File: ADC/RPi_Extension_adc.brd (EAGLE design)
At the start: 63 x 50 mm, 39 parts, among them U1 74AHC1G04GW/T1, U2 ADR423ARZ, U3 AD7616BSTZ

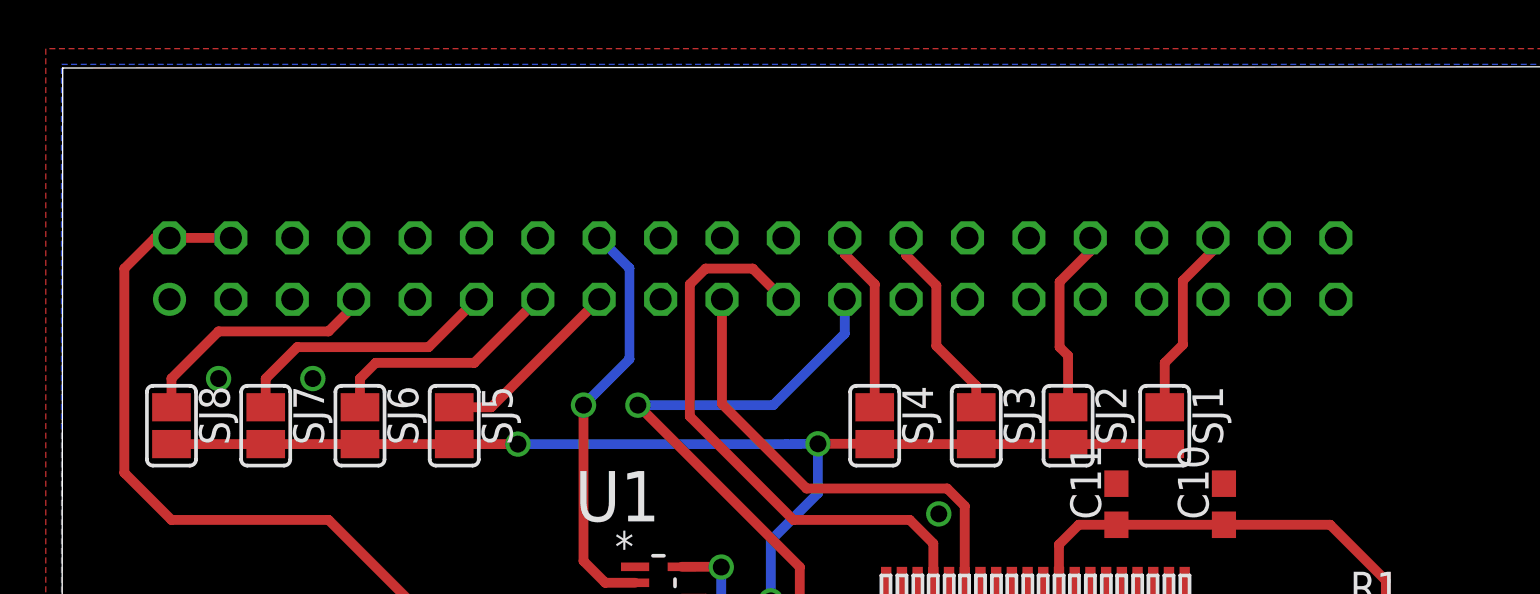
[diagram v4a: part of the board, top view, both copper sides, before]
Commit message: added additional id jumpers to adc and dac board
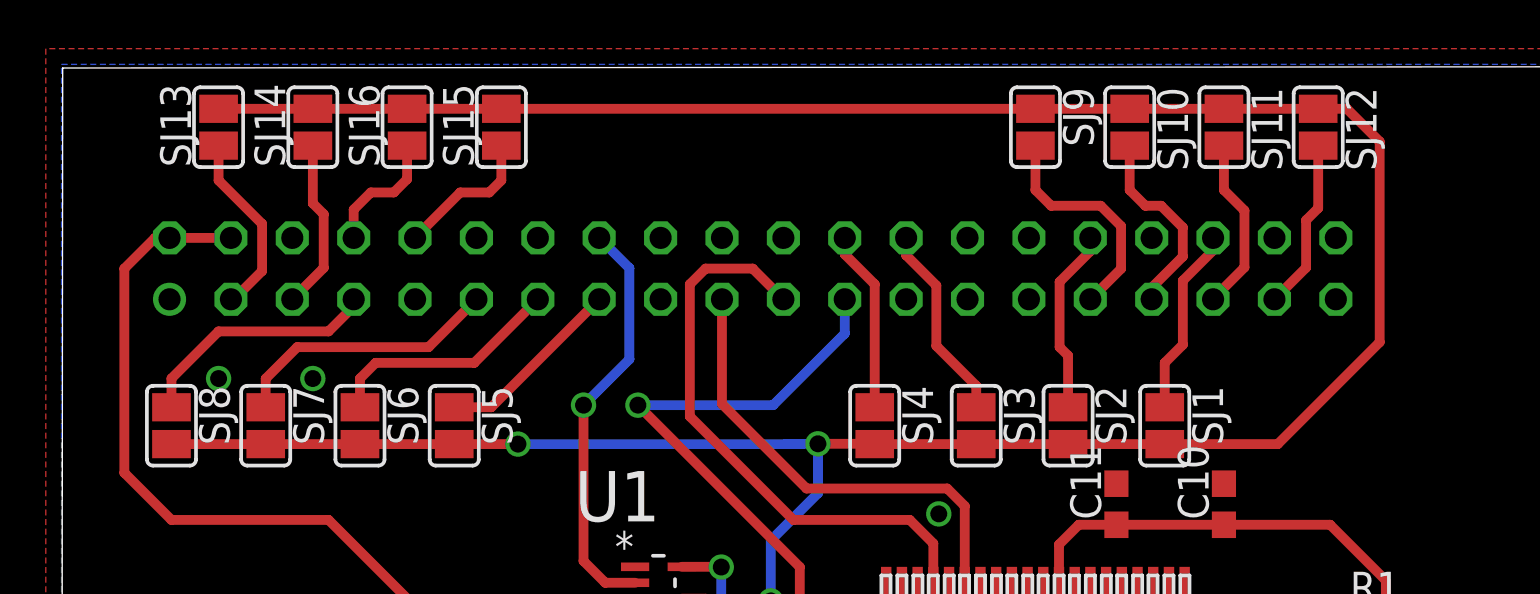
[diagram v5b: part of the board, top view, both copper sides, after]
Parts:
- added SJ10, SJ11, SJ12, SJ13, SJ14, SJ15, SJ16, SJ9: (no value), jumper:SJ
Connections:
- new net N$11: SJ15.1, SV5.10
- new net N$12: SJ9.2, SV5.31
- new net N$13: SJ10.2, SV5.33
- new net N$14: SJ11.2, SV5.35
- new net N$15: SJ12.2, SV5.37
- new net N$5: SJ13.1, SV5.3
- new net N$8: SJ14.1, SV5.5
- new net N$9: SJ16.1, SV5.8
- net SYNC: now also SJ10.1, SJ11.1, SJ12.1, SJ13.2, SJ14.2, SJ15.2, SJ16.2, SJ9.1
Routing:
- net SYNC: track 53.2 -> 120.7 mm
- net N$12: track 0.00 -> 9.56 mm
- net N$13: track 0.00 -> 8.18 mm
- net N$5: track 0.00 -> 7.71 mm
- net N$14: track 0.00 -> 7.25 mm
- net N$15: track 0.00 -> 7.11 mm
- net N$8: track 0.00 -> 7.08 mm
- net N$11: track 0.00 -> 6.00 mm
- net N$9: track 0.00 -> 5.29 mm
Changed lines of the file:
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@@
 <attribute name="OC_NEWARK" value="99K0513" x="24.7" y="28.6" size="1.778" layer="27" display="off"/>
 </element>
+<element name="SJ9" library="jumper" package="SJ" value="" x="40.3" y="47.45" rot="R270"/>
+<element name="SJ10" library="jumper" package="SJ" value="" x="44.2" y="47.45" rot="R270"/>
+<element name="SJ11" library="jumper" package="SJ" value="" x="48.1" y="47.45" rot="R270"/>
+<element name="SJ12" library="jumper" package="SJ" value="" x="52" y="47.45" rot="R270"/>
+<element name="SJ13" library="jumper" package="SJ" value="" x="6.5" y="47.45" rot="R90"/>
+<element name="SJ14" library="jumper" package="SJ" value="" x="10.4" y="47.45" rot="R90"/>
+<element name="SJ15" library="jumper" package="SJ" value="" x="18.2" y="47.45" rot="R90"/>
+<element name="SJ16" library="jumper" package="SJ" value="" x="14.3" y="47.45" rot="R90"/>
 </elements>
 <signals>
@@
 <wire x1="31.3" y1="32.3" x2="29.35" y2="30.35" width="0.4064" layer="16"/>
 <wire x1="29.35" y1="30.35" x2="29.35" y2="27.85" width="0.4064" layer="16"/>
+<contactref element="SJ14" pad="2"/>
+<contactref element="SJ15" pad="2"/>
+<contactref element="SJ16" pad="2"/>
+<contactref element="SJ13" pad="2"/>
+<contactref element="SJ9" pad="1"/>
+<contactref element="SJ10" pad="1"/>
+<contactref element="SJ11" pad="1"/>
+<contactref element="SJ12" pad="1"/>
+<wire x1="6.5" y1="48.212" x2="10.4" y2="48.212" width="0.4064" layer="1"/>
+<wire x1="10.4" y1="48.212" x2="14.3" y2="48.212" width="0.4064" layer="1"/>
+<wire x1="14.3" y1="48.212" x2="18.2" y2="48.212" width="0.4064" layer="1"/>
+<wire x1="18.2" y1="48.212" x2="40.3" y2="48.212" width="0.4064" layer="1"/>
+<wire x1="40.3" y1="48.212" x2="44.2" y2="48.212" width="0.4064" layer="1"/>
+<wire x1="44.2" y1="48.212" x2="48.1" y2="48.212" width="0.4064" layer="1"/>
+<wire x1="52" y1="48.212" x2="53.188" y2="48.212" width="0.4064" layer="1"/>
+<wire x1="45.65" y1="34.338" x2="50.328315625" y2="34.338" width="0.4064" layer="1"/>
+<wire x1="50.328315625" y1="34.338" x2="54.5448875" y2="38.554571875" width="0.4064" layer="1"/>
+<wire x1="54.5448875" y1="38.554571875" x2="54.5448875" y2="46.8551125" width="0.4064" layer="1"/>
+<wire x1="54.5448875" y1="46.8551125" x2="53.188" y2="48.212" width="0.4064" layer="1"/>
+<wire x1="52" y1="48.212" x2="48.1" y2="48.212" width="0.4064" layer="1"/>
 </signal>
 <signal name="N$20">
@@
 <wire x1="30.55" y1="23.05" x2="31.175" y2="22.425" width="0.4064" layer="1"/>
 </signal>
+<signal name="N$5">
+<contactref element="SV5" pad="3"/>
+<contactref element="SJ13" pad="1"/>
+<wire x1="7.01" y1="40.33" x2="7.13" y2="40.33" width="0.4064" layer="1"/>
+<wire x1="7.13" y1="40.33" x2="8.3" y2="41.5" width="0.4064" layer="1"/>
+<wire x1="8.3" y1="41.5" x2="8.3" y2="43.45" width="0.4064" layer="1"/>
+<wire x1="8.3" y1="43.45" x2="6.5" y2="45.25" width="0.4064" layer="1"/>
+<wire x1="6.5" y1="45.25" x2="6.5" y2="46.688" width="0.4064" layer="1"/>
+</signal>
+<signal name="N$8">
+<contactref element="SV5" pad="5"/>
+<contactref element="SJ14" pad="1"/>
+<wire x1="10.4" y1="46.688" x2="10.4" y2="44.3" width="0.4064" layer="1"/>
+<wire x1="10.4" y1="44.3" x2="10.85" y2="43.85" width="0.4064" layer="1"/>
+<wire x1="10.85" y1="43.85" x2="10.85" y2="41.63" width="0.4064" layer="1"/>
+<wire x1="10.85" y1="41.63" x2="9.55" y2="40.33" width="0.4064" layer="1"/>
+</signal>
+<signal name="N$9">
+<contactref element="SV5" pad="8"/>
+<contactref element="SJ16" pad="1"/>
+<wire x1="12.09" y1="42.87" x2="12.09" y2="44.04" width="0.4064" layer="1"/>
+<wire x1="12.09" y1="44.04" x2="12.8" y2="44.75" width="0.4064" layer="1"/>
+<wire x1="12.8" y1="44.75" x2="13.75" y2="44.75" width="0.4064" layer="1"/>
+<wire x1="13.75" y1="44.75" x2="14.3" y2="45.3" width="0.4064" layer="1"/>
+<wire x1="14.3" y1="45.3" x2="14.3" y2="46.688" width="0.4064" layer="1"/>
+</signal>
+<signal name="N$11">
+<contactref element="SV5" pad="10"/>
+<contactref element="SJ15" pad="1"/>
+<wire x1="14.63" y1="42.87" x2="14.63" y2="42.88" width="0.4064" layer="1"/>
+<wire x1="14.63" y1="42.88" x2="16.5" y2="44.75" width="0.4064" layer="1"/>
+<wire x1="16.5" y1="44.75" x2="17.7" y2="44.75" width="0.4064" layer="1"/>
+<wire x1="17.7" y1="44.75" x2="18.2" y2="45.25" width="0.4064" layer="1"/>
+<wire x1="18.2" y1="45.25" x2="18.2" y2="46.688" width="0.4064" layer="1"/>
+</signal>
+<signal name="N$12">
+<contactref element="SV5" pad="31"/>
+<contactref element="SJ9" pad="2"/>
+<wire x1="42.57" y1="40.33" x2="42.58" y2="40.33" width="0.4064" layer="1"/>
+<wire x1="42.58" y1="40.33" x2="43.842459375" y2="41.592459375" width="0.4064" layer="1"/>
+<wire x1="43.842459375" y1="41.592459375" x2="43.842459375" y2="43.3567875" width="0.4064" layer="1"/>
+<wire x1="43.842459375" y1="43.3567875" x2="42.999246875" y2="44.2" width="0.4064" layer="1"/>
+<wire x1="42.999246875" y1="44.2" x2="40.95" y2="44.2" width="0.4064" layer="1"/>
+<wire x1="40.95" y1="44.2" x2="40.3" y2="44.85" width="0.4064" layer="1"/>
+<wire x1="40.3" y1="44.85" x2="40.3" y2="46.688" width="0.4064" layer="1"/>
+</signal>
+<signal name="N$13">
+<contactref element="SV5" pad="33"/>
+<contactref element="SJ10" pad="2"/>
+<wire x1="45.11" y1="40.33" x2="45.11" y2="40.81" width="0.4064" layer="1"/>
+<wire x1="45.11" y1="40.81" x2="46.397921875" y2="42.097921875" width="0.4064" layer="1"/>
+<wire x1="46.397921875" y1="42.097921875" x2="46.397921875" y2="43.302078125" width="0.4064" layer="1"/>
+<wire x1="46.397921875" y1="43.302078125" x2="45.5" y2="44.2" width="0.4064" layer="1"/>
+<wire x1="45.5" y1="44.2" x2="44.85" y2="44.2" width="0.4064" layer="1"/>
+<wire x1="44.85" y1="44.2" x2="44.2" y2="44.85" width="0.4064" layer="1"/>
+<wire x1="44.2" y1="44.85" x2="44.2" y2="46.688" width="0.4064" layer="1"/>
+</signal>
+<signal name="N$14">
+<contactref element="SV5" pad="35"/>
+<contactref element="SJ11" pad="2"/>
+<wire x1="47.65" y1="40.33" x2="47.65" y2="40.35" width="0.4064" layer="1"/>
+<wire x1="47.65" y1="40.35" x2="48.95" y2="41.65" width="0.4064" layer="1"/>
+<wire x1="48.95" y1="41.65" x2="48.95" y2="44" width="0.4064" layer="1"/>
+<wire x1="48.95" y1="44" x2="48.1" y2="44.85" width="0.4064" layer="1"/>
+<wire x1="48.1" y1="44.85" x2="48.1" y2="46.688" width="0.4064" layer="1"/>
+</signal>
+<signal name="N$15">
+<contactref element="SV5" pad="37"/>
+<contactref element="SJ12" pad="2"/>
+<wire x1="52" y1="46.688" x2="52" y2="44.1" width="0.4064" layer="1"/>
+<wire x1="52" y1="44.1" x2="51.5" y2="43.6" width="0.4064" layer="1"/>
+<wire x1="51.5" y1="43.6" x2="51.5" y2="41.64" width="0.4064" layer="1"/>
+<wire x1="51.5" y1="41.64" x2="50.19" y2="40.33" width="0.4064" layer="1"/>
+</signal>
 </signals>

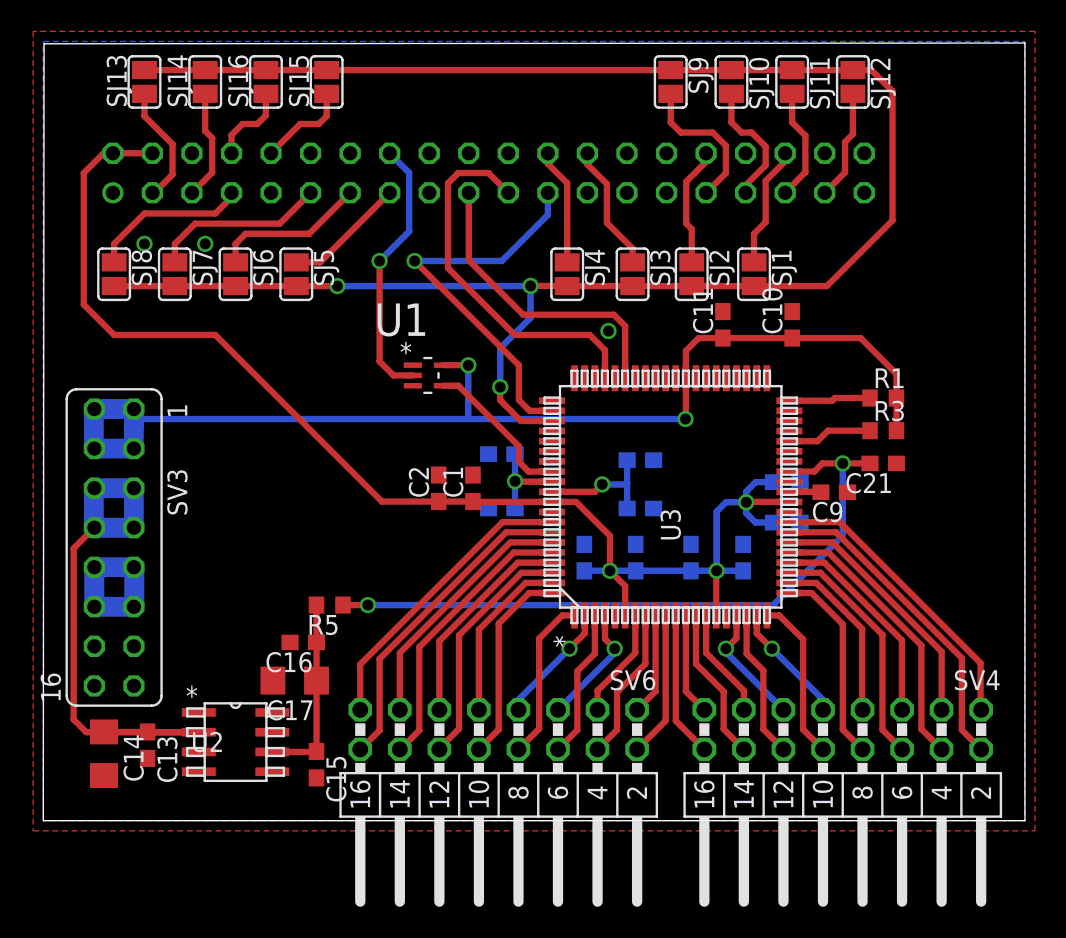
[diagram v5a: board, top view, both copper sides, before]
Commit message: fixed severe bug on adc board
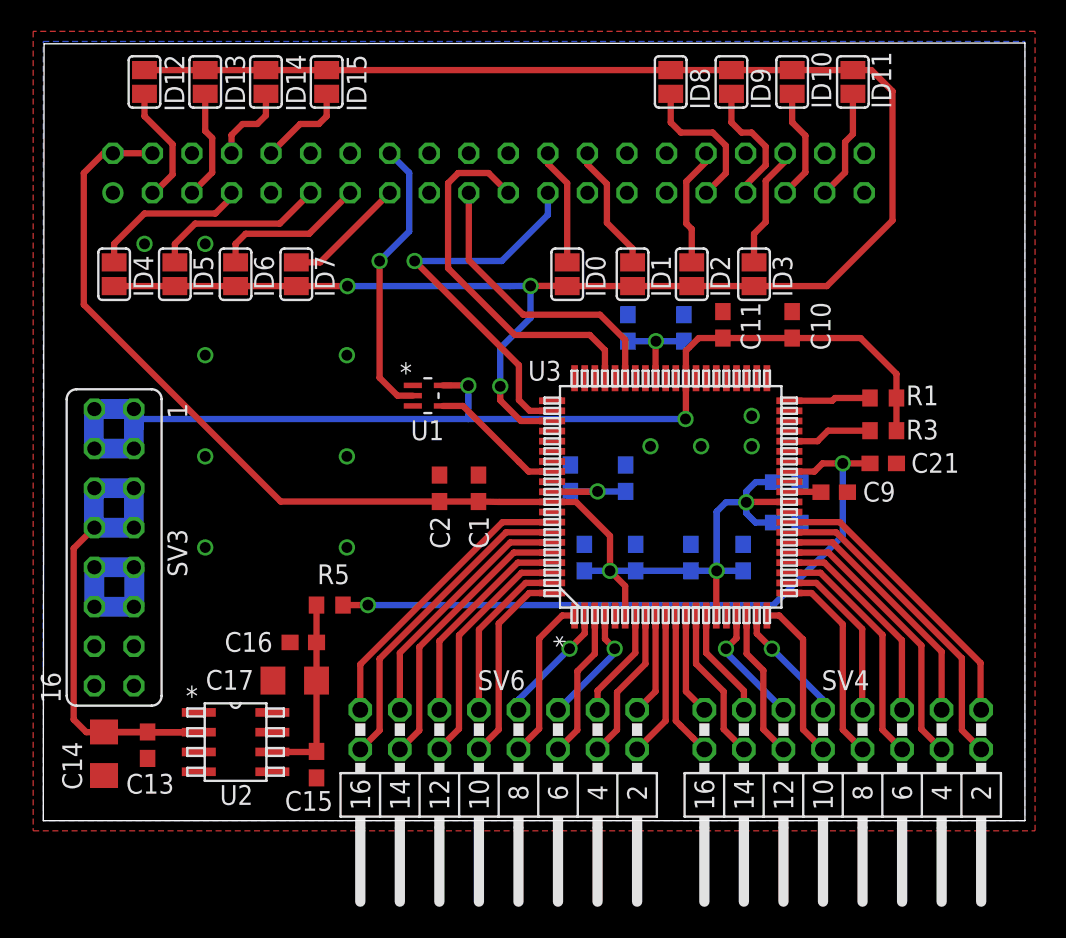
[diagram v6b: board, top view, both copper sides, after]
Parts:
- moved C20 14.2 mm to (41.1, 31.6), turned to 90 degrees
- moved C19 14.1 mm to (37.5, 31.6), turned to 90 degrees
- moved C12 4.64 mm to (33.9, 22.0), turned to 90 degrees
- moved C18 2.17 mm to (37.4, 22.0), turned to 90 degrees
- moved U1 1.30 mm to (24.7, 27.3)
- moved C1 0.35 mm to (27.9, 21.4)
- moved C2 0.05 mm to (25.4, 21.4)
- renumbered SJ1 to ID3, SJ10 to ID9, SJ11 to ID10, SJ12 to ID11, SJ13 to ID12, SJ14 to ID13, SJ15 to ID15, SJ16 to ID14, SJ2 to ID2, SJ3 to ID1, SJ4 to ID0, SJ5 to ID7, SJ6 to ID6, SJ7 to ID5, SJ8 to ID4, SJ9 to ID8
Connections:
- removed net N$1 (its old number): C19.1, C20.1, U3.69
- new net N$16: C19.1, C20.1, U3.52
- net GND: now also U3.69; no longer U3.52
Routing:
- net N$16: track 0.00 -> 5.99 mm, vias 0 -> 1
- net N$1 (its old number): track 5.89 -> 0.00 mm, vias 1 -> 0
- net N$1: track 8.16 -> 6.48 mm
- net VDRIVE: track 76.1 -> 74.8 mm
- net CONVST: track 17.2 -> 18.3 mm
- net N$3: track 9.88 -> 8.76 mm
- net MOSI: track 19.5 -> 19.0 mm
